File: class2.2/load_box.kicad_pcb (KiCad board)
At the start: 2 copper layers, 16 parts, among them J1 CONN_01X02, J2 CONN_01X02, U1 STM32L152C6TxA, Y1 Crystal_GND24

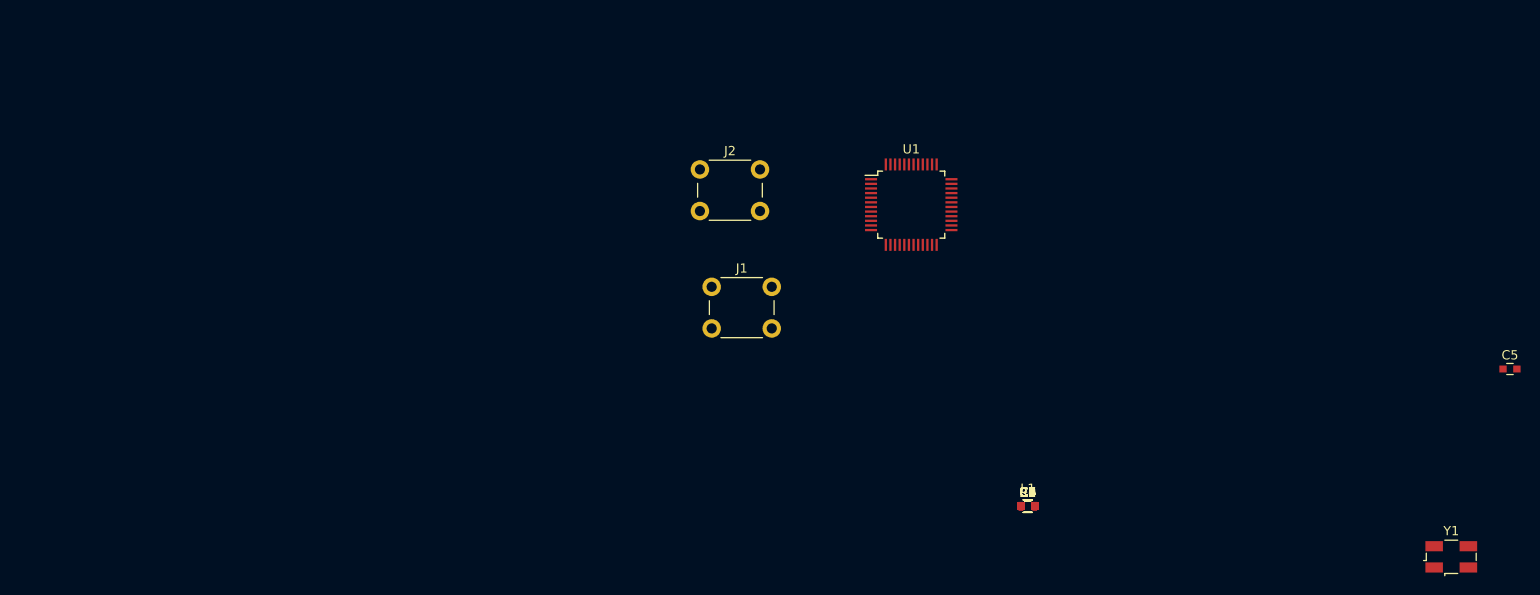
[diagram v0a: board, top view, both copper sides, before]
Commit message: Moving class2.2 forward, includes 13V switching converter.
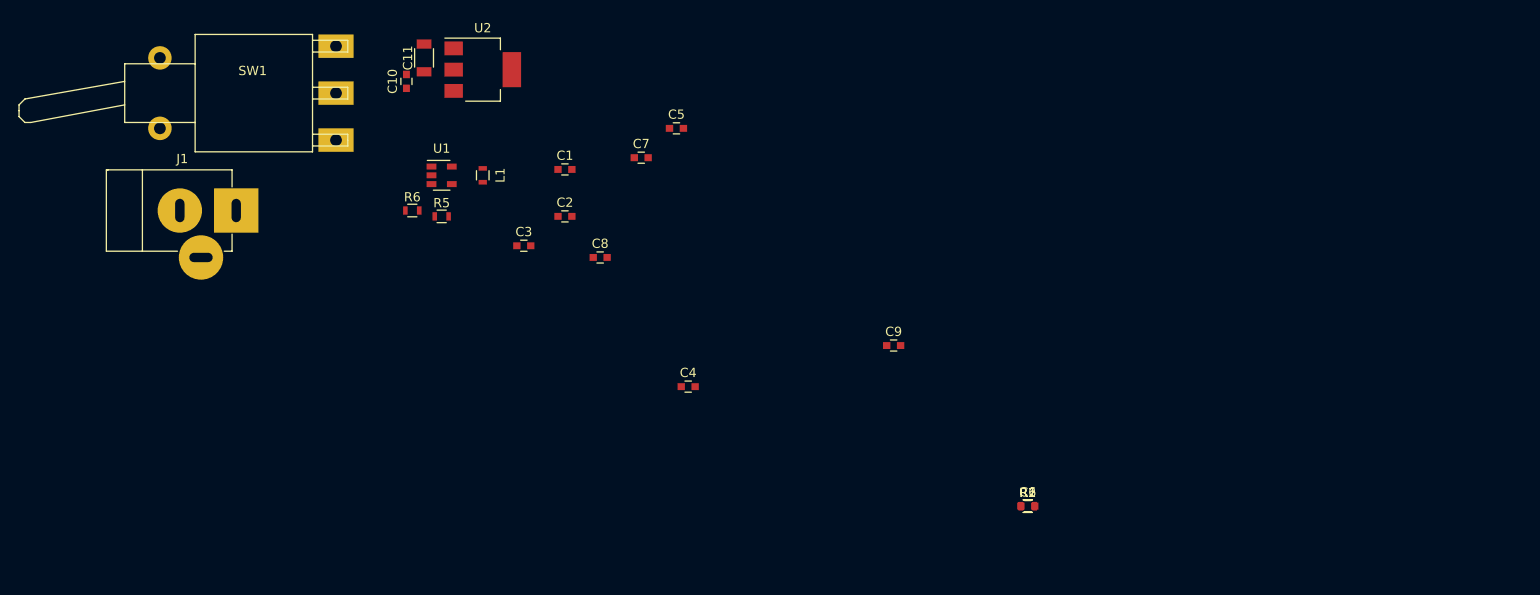
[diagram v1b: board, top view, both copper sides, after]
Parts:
- removed J2: CONN_01X02, Buttons_Switches_THT:SW_PUSH_6mm_h9.5mm
- removed Y1: Crystal_GND24, Crystals:Crystal_SMD_EuroQuartz_MJ-4pin_5.0x3.2mm
- added C10: 0.1u, Capacitors_SMD:C_0603, F.Cu at (81.3, 59.1)
- added C11: 10u, Capacitors_SMD:C_1206, F.Cu at (83.2, 56.5)
- added R5: 90.9k, Resistors_SMD:R_0603, F.Cu at (85.1, 73.7)
- added R6: 8.45k, Resistors_SMD:R_0603, F.Cu at (81.9, 73.0)
- added SW1: SW_SPST, Buttons_Switches_THT:SW_SPDT, F.Cu at (73.7, 60.3)
- added U2: LD1117S33TR, TO_SOT_Packages_SMD:SOT-223, F.Cu at (89.5, 57.8)
- C7, C8: value C -> 1u
- J1: value CONN_01X02 -> BARREL_JACK; footprint Buttons_Switches_THT:SW_PUSH_6mm_h9.5mm -> Connectors:JACK_ALIM
- L1: value Ferrite_Bead -> 10uH
- U1: value STM32L152C6TxA -> AP3012; footprint Housings_QFP:LQFP-48_7x7mm_Pitch0.5mm -> TO_SOT_Packages_SMD:SOT-23-5
- moved C5 93.9 mm to (110.5, 64.1)
- moved L1 69.0 mm to (89.5, 69.2), turned to 270 degrees
- moved C1 61.9 mm to (98.4, 68.6)
- moved C3 61.4 mm to (94.0, 76.8)
- moved C2 59.1 mm to (98.4, 73.7)
- moved C7 56.3 mm to (106.7, 67.3)
- moved C8 53.5 mm to (102.2, 78.1)
- moved J1 52.1 mm to (62.9, 73.0)
- moved U1 50.9 mm to (85.1, 69.2)
- moved C4 38.9 mm to (111.8, 92.1)
- moved C9 22.6 mm to (134.0, 87.6)
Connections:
- C1 pad 1: Net-(C1-Pad1) -> GND
- C1 pad 2: GND -> (no net)
- C2 pad 1: Net-(C2-Pad1) -> GND
- C2 pad 2: GND -> +3V3
- C3 pad 1: Net-(C3-Pad1) -> GND
- C3 pad 2: Net-(C3-Pad2) -> +3V3
- C4 pad 1: RSTB -> (no net)
- C5 pad 1: +5V -> +3V3
- C6 pad 1: +5V -> (no net)
- C7 pad 1: +5V -> +12V
- C8 pad 1: +5V -> /load_box_power/+13V
- J1 pad 1: GND -> Net-(J1-Pad1)
- J1 pad 2: RSTB -> GND
- L1 pad 1: +5V -> +12V
- L1 pad 2: AVDD -> Net-(D3-Pad2)
- R1 pad 1: +5V -> (no net)
- U1 pad 1: Net-(U1-Pad1) -> Net-(D3-Pad2)
- U1 pad 2: USERB -> GND
- U1 pad 3: Net-(C1-Pad1) -> Net-(R5-Pad2)
- U1 pad 4: Net-(C2-Pad1) -> +3V3
- U1 pad 5: Net-(U1-Pad5) -> +12V
